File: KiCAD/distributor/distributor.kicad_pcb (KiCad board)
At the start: 4 copper layers, 235 x 29 mm, 12 parts, among them P1 CONN_02X03, P11 CONN_02X03, P13 CONN_02X03, P15 CONN_02X03, P17 CONN_02X03, P19 CONN_02X03, P21 CONN_02X22, P3 CONN_02X03, P5 CONN_02X03, P7 CONN_02X03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

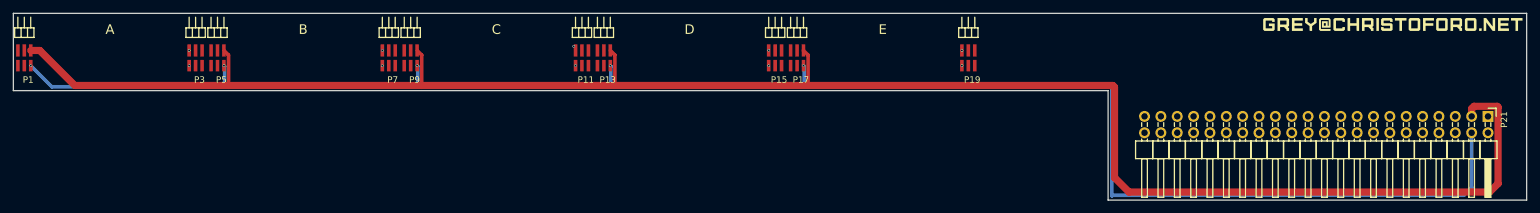
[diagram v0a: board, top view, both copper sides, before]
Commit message: 1x distro board wired
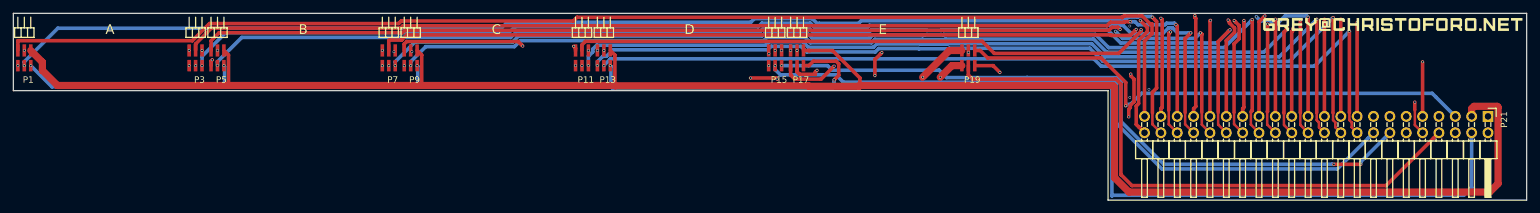
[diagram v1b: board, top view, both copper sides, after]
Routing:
- net A2_V: track 0.00 -> 198.6 mm, vias 0 -> 2
- net A0_V: track 0.00 -> 197.3 mm, vias 0 -> 2
- net A2_I: track 0.00 -> 195.2 mm, vias 0 -> 2
- net A0_I: track 0.00 -> 194.6 mm
- net B2_V: track 0.00 -> 179.6 mm, vias 0 -> 2
- net B2_I: track 0.00 -> 177.0 mm, vias 0 -> 2
- net AR_V: track 0.00 -> 175.4 mm, vias 0 -> 2
- net B0_I: track 0.00 -> 174.3 mm, vias 0 -> 2
- net B0_V: track 0.00 -> 173.9 mm, vias 0 -> 3
- net AR_I: track 0.00 -> 173.3 mm, vias 0 -> 3
- net A4_V: track 0.00 -> 172.2 mm, vias 0 -> 2
- net A4_I: track 0.00 -> 169.4 mm, vias 0 -> 2
- net C2_V: track 0.00 -> 158.4 mm, vias 0 -> 2
- net BR_V: track 0.00 -> 157.0 mm, vias 0 -> 2
- net C0_V: track 0.00 -> 156.6 mm, vias 0 -> 2
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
